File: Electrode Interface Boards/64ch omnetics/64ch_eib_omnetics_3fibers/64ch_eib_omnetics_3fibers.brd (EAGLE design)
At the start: 16.5 x 16.5 mm, 2 parts

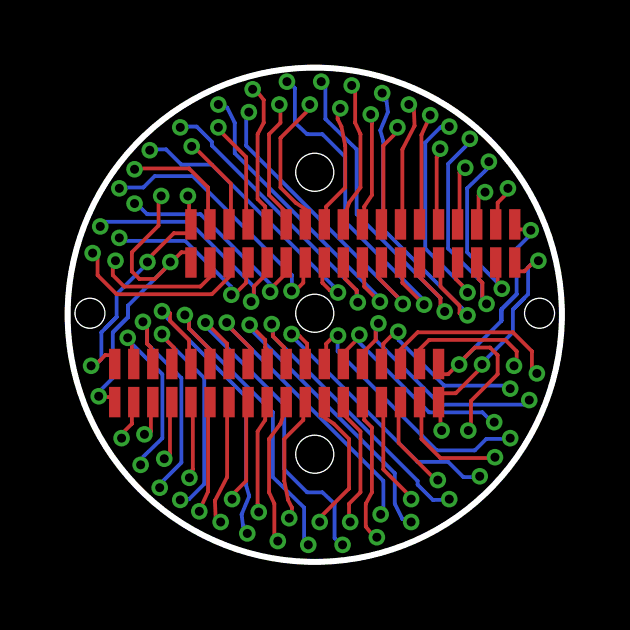
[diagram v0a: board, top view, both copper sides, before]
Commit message: fixed drc errors
changed mounting holes to 0.762mm
moved some electrode pin vias away from edge
re-routed central traces around ferrule hole
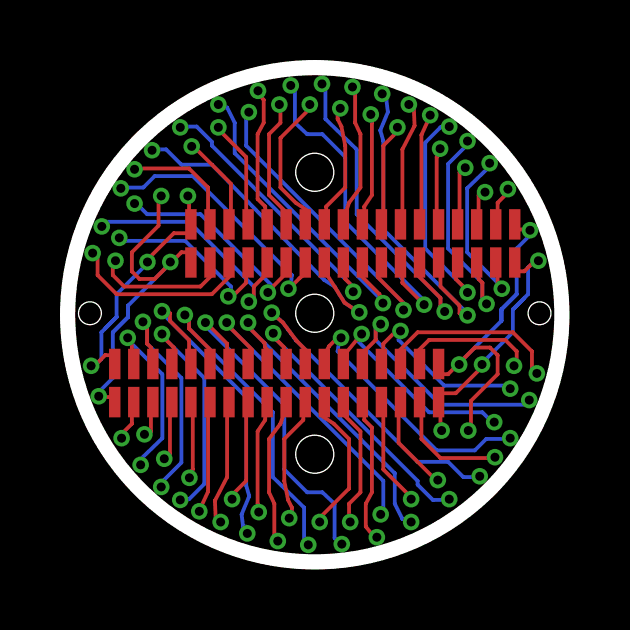
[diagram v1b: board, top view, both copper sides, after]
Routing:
- net S$102: track 8.12 -> 9.23 mm
- net S$116: track 8.12 -> 9.18 mm
- net S$31: track 0.74 -> 1.73 mm
- net S$10: track 0.74 -> 1.63 mm
